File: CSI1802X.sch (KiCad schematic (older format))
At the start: 19 parts

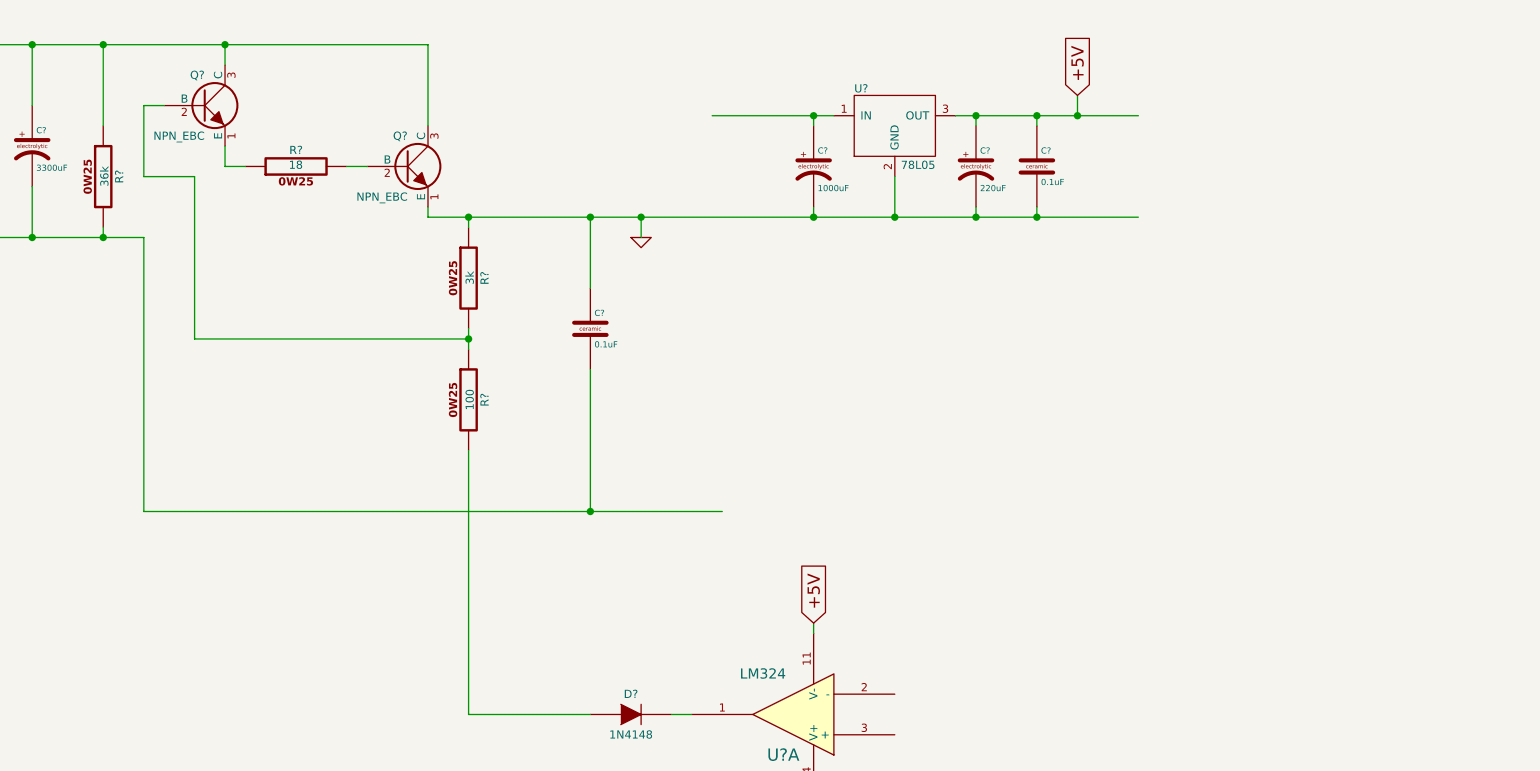
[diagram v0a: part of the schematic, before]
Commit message: -5V rail.
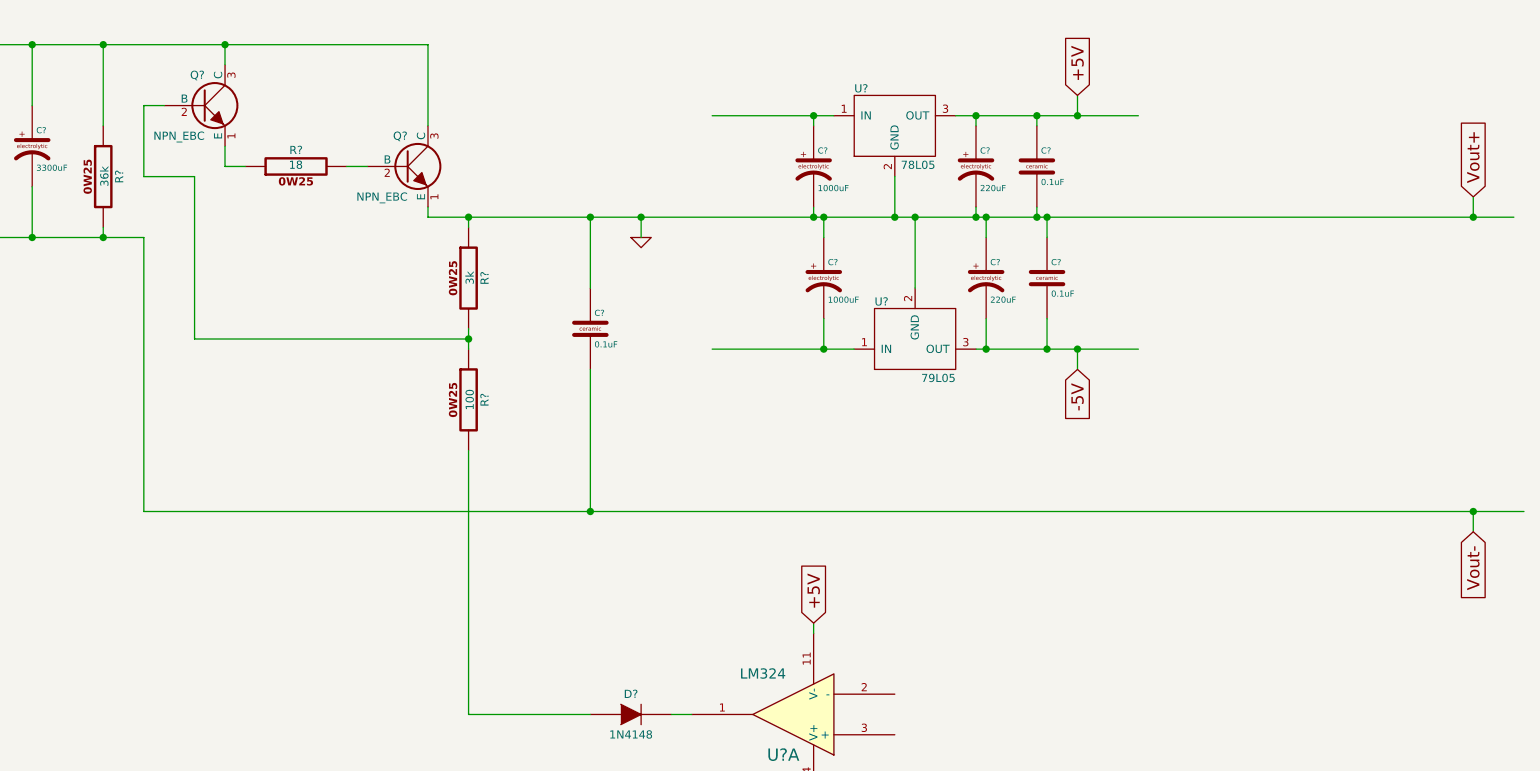
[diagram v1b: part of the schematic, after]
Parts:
- added C?: 1000uF, ~, symbol C_EL
- added C?: 220uF, ~, symbol C_EL
- added C?: 0.1uF, ~, symbol C_CER
- added U?: 79L05, ~, symbol 79L05
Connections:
- net labels added: -5V, Vout+, Vout-
- wire segments 51 -> 63
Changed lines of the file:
@@
 $EndComp
 Wire Wire Line
-	6200 2650 9700 2650
+	6200 2650 11550 2650
 $Comp
 L C_CER C?
@@
 Connection ~ 7000 2650
 Wire Wire Line
-	4800 4100 7650 4100
+	4800 4100 11600 4100
 Wire Wire Line
 	4800 2750 4800 4100
@@
 Wire Wire Line
 	8100 4700 8100 4650
+$Comp
+L 79L05 U?
+U 1 1 533A1DC9
+P 8600 3250
+F 0 "U?" H 8400 3410 40  0000 L BNN
+F 1 "79L05" H 8800 3080 40  0000 R TNN
+F 2 "~" H 8600 3250 60  0000 C CNN
+F 3 "~" H 8600 3250 60  0000 C CNN
+	1    8600 3250
+	1    0    0    -1
+$EndComp
+$Comp
+L C_EL C?
+U 1 1 533A1DD6
+P 8150 2950
+F 0 "C?" H 8170 3010 30  0000 L BNN
+F 1 "1000uF" H 8170 2860 30  0000 L TNN
+F 2 "~" H 8188 2800 30  0000 C CNN
+F 3 "~" H 8150 2950 60  0000 C CNN
+	1    8150 2950
+	1    0    0    -1
+$EndComp
+$Comp
+L C_EL C?
+U 1 1 533A1DE6
+P 8950 2950
+F 0 "C?" H 8970 3010 30  0000 L BNN
+F 1 "220uF" H 8970 2860 30  0000 L TNN
+F 2 "~" H 8988 2800 30  0000 C CNN
+F 3 "~" H 8950 2950 60  0000 C CNN
+	1    8950 2950
+	1    0    0    -1
+$EndComp
+$Comp
+L C_CER C?
+U 1 1 533A1DEC
+P 9250 2950
+F 0 "C?" H 9270 3010 30  0000 L BNN
+F 1 "0.1uF" H 9270 2890 30  0000 L TNN
+F 2 "~" H 9288 2800 30  0000 C CNN
+F 3 "~" H 9250 2950 60  0000 C CNN
+	1    9250 2950
+	1    0    0    -1
+$EndComp
+Wire Wire Line
+	8300 3300 7600 3300
+Wire Wire Line
+	8900 3300 9700 3300
+Wire Wire Line
+	9250 2750 9250 2650
+Connection ~ 9250 2650
+Wire Wire Line
+	8950 2750 8950 2650
+Connection ~ 8950 2650
+Wire Wire Line
+	8150 2750 8150 2650
+Connection ~ 8150 2650
+Wire Wire Line
+	8150 3150 8150 3300
+Connection ~ 8150 3300
+Wire Wire Line
+	8950 3150 8950 3300
+Connection ~ 8950 3300
+Wire Wire Line
+	9250 3150 9250 3300
+Connection ~ 9250 3300
+Text GLabel 9400 3400 3    60   Input ~ 0
+-5V
+Wire Wire Line
+	9400 3400 9400 3300
+Connection ~ 9400 3300
+Wire Wire Line
+	8600 3000 8600 2650
+Connection ~ 8600 2650
+Text GLabel 11350 2550 1    60   Input ~ 0
+Vout+
+Wire Wire Line
+	11350 2550 11350 2650
+Connection ~ 11350 2650
+Text GLabel 11350 4200 3    60   Input ~ 0
+Vout-
+Wire Wire Line
+	11350 4200 11350 4100
+Connection ~ 11350 4100
 $EndSCHEMATC

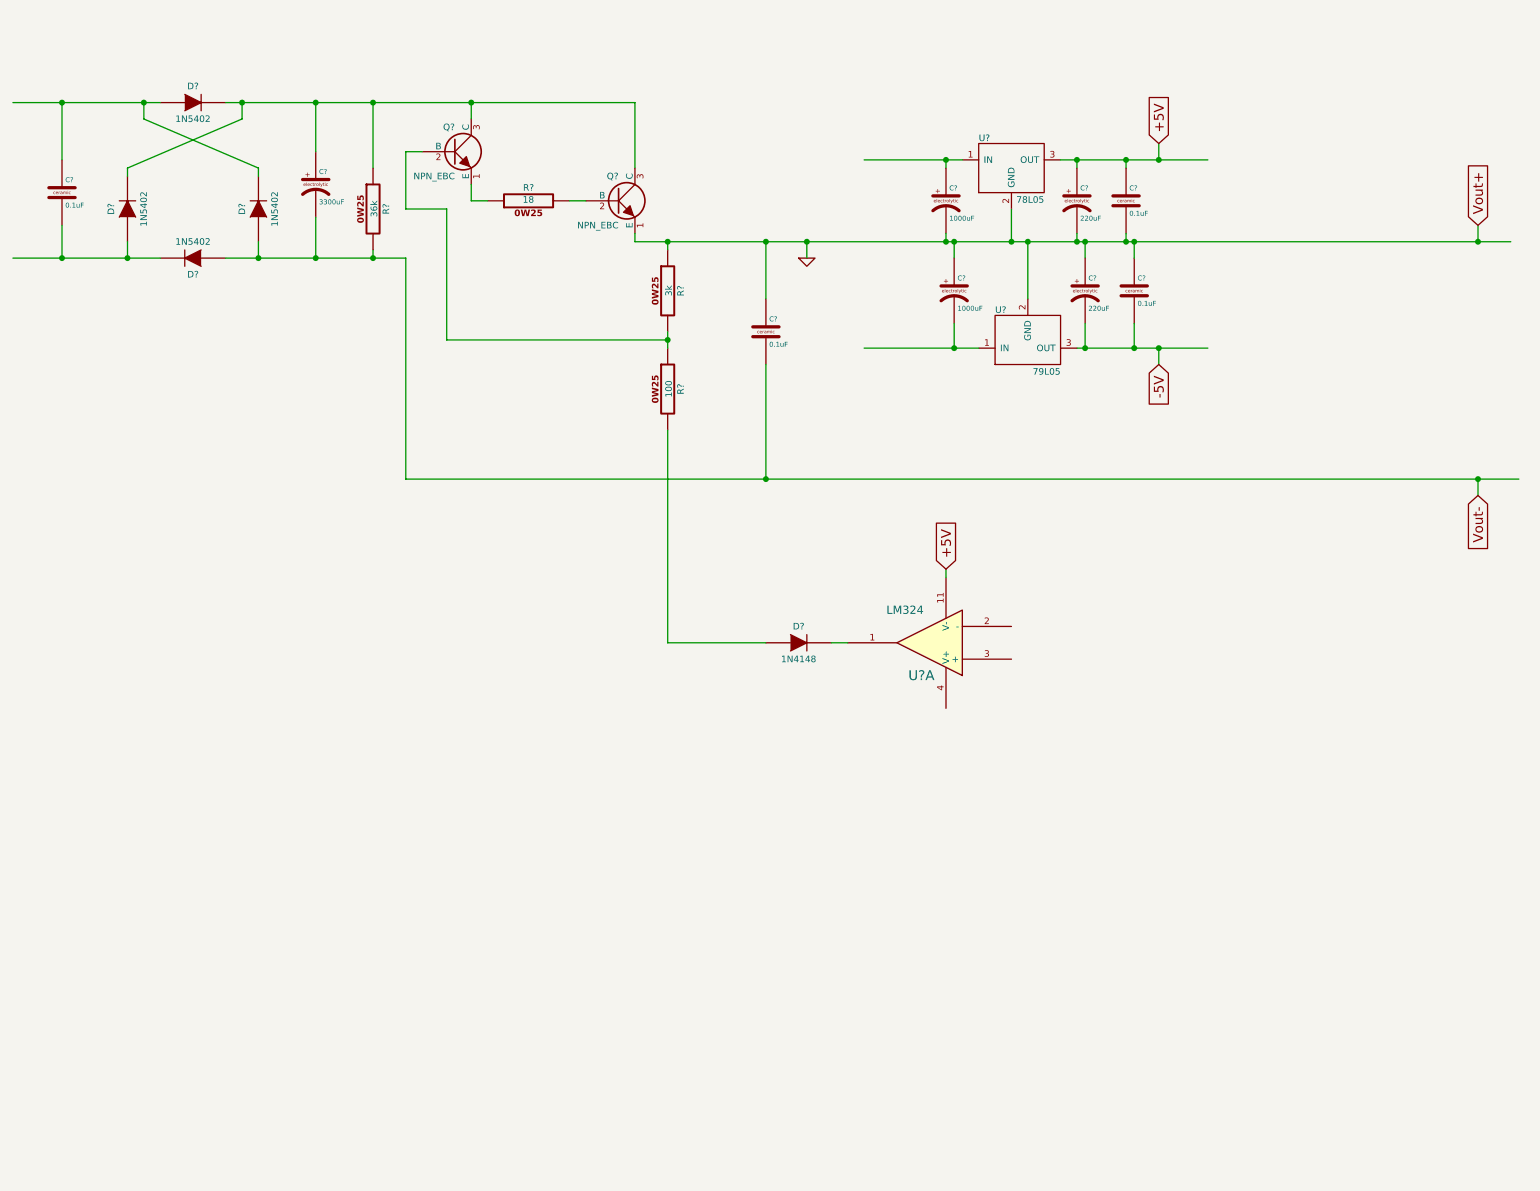
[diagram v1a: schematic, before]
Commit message: fleshing out op amp section
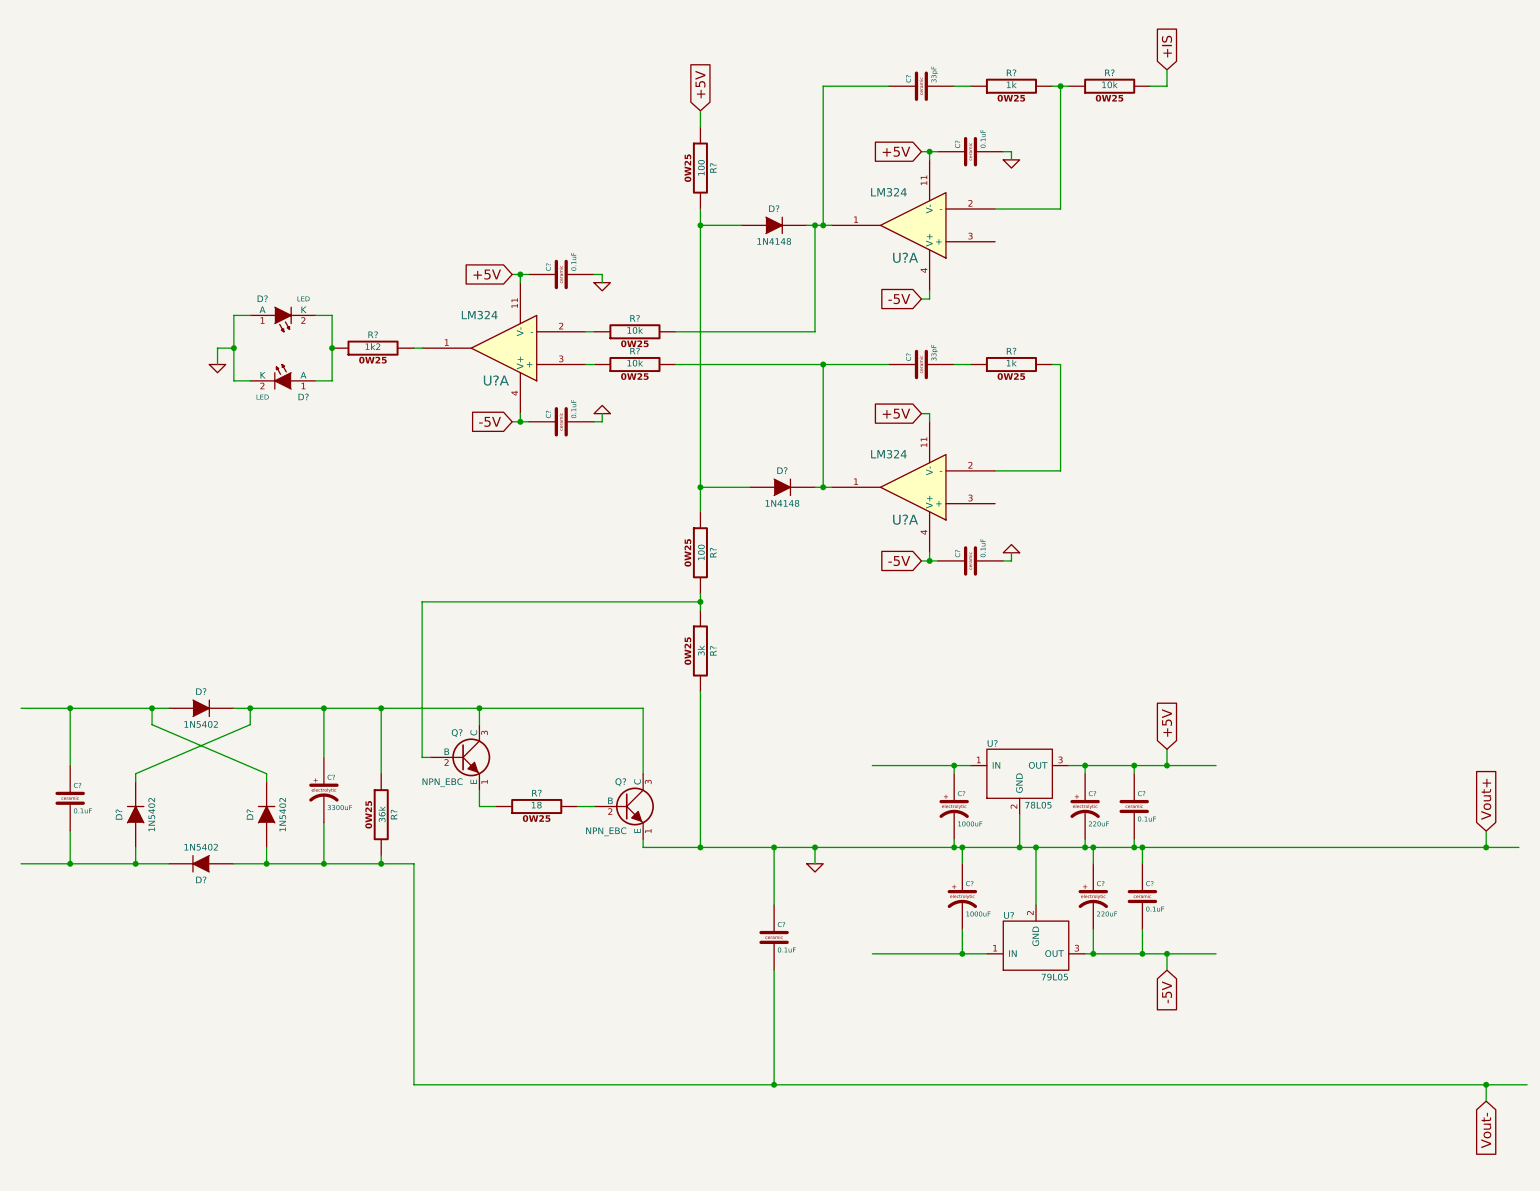
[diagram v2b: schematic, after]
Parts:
- added C? (x4): 0.1uF, ~, symbol C_CER
- added C? (x2): 33pF, ~, symbol C_CER
- added D?: 1N4148, ~, symbol DIODE
- added D? (x2): LED, ~, symbol LED
- added R?: 100, ~, symbol R_0W25
- added R? (x3): 10k, ~, symbol R_0W25
- added R? (x2): 1k, ~, symbol R_0W25
- added R?: 1k2, ~, symbol R_0W25
- added U? (x2): LM324, symbol LM324
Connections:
- net labels added: +IS
- wire segments 63 -> 110
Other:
- moved on the sheet: C?, D?, Q?, R?, U?, U?A

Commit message: fleshing out resistive dividers
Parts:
- added C?: 220uF, ~, symbol C_EL
- added C? (x3): 0.1uF, ~, symbol C_CER
- added D?: 1N4007, ~, symbol DIODE
- added R?: 0.1, ~, symbol R_0W25
- added R? (x5): 10k, ~, symbol R_0W25
- added R? (x2): 820, ~, symbol R_0W25
- added R? (x2): 180, ~, symbol R_0W25
- added R? (x2): 4k7, ~, symbol R_0W25
- added R?: 3k9, ~, symbol R_0W25
- added R?: 1k8, ~, symbol R_0W25
- added RV? (x2): 10k, ~, symbol POT
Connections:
- net labels added: +VS, -VS, REF
- net labels removed: Vout+, Vout-
- wire segments 110 -> 154
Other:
- moved on the sheet: C?, R?, U?

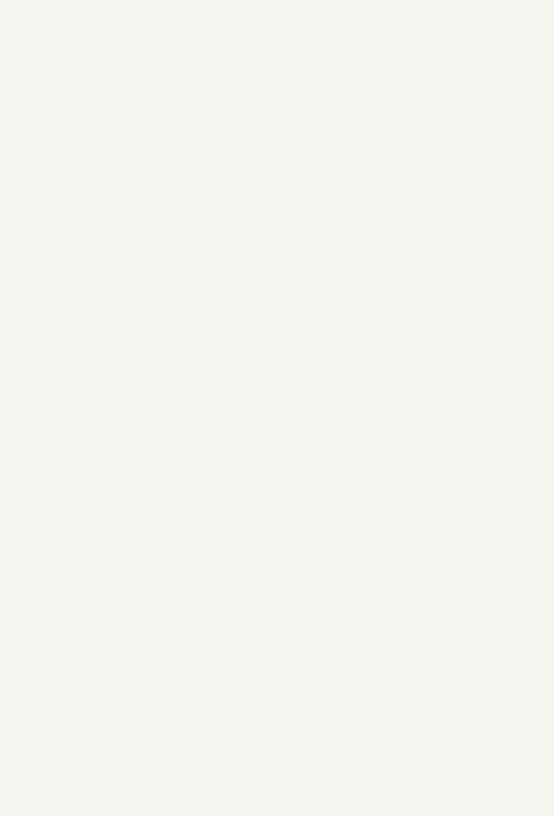
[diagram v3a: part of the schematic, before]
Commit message: TL431 regulator (REF)
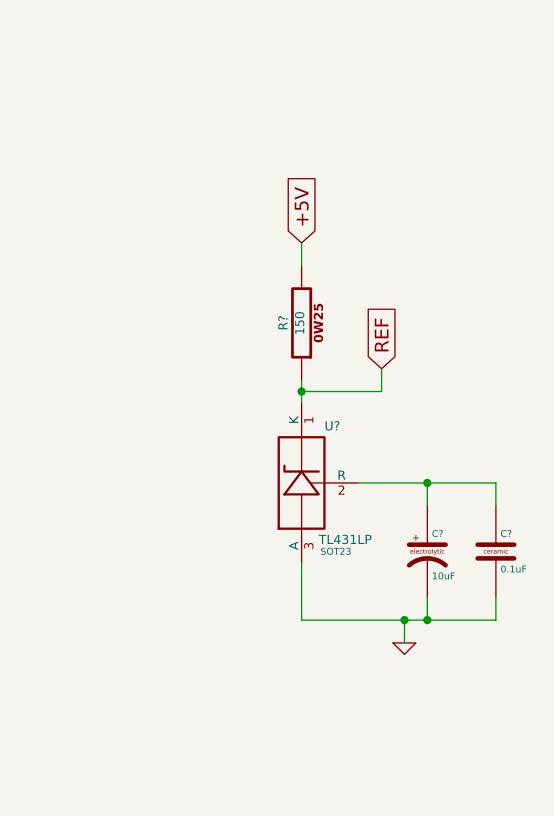
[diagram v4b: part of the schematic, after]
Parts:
- added C?: 10uF, ~, symbol C_EL
- added C?: 0.1uF, ~, symbol C_CER
- added R?: 150, ~, symbol R_0W25
- added U?: TL431LP, SOT23, symbol TL431LP
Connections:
- wire segments 154 -> 166
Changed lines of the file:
@@
 Wire Wire Line
 	12200 3450 12200 3400
+$Comp
+L TL431LP U?
+U 1 1 533A7045
+P 14850 4850
+F 0 "U?" H 14950 5075 40  0000 L BNN
+F 1 "TL431LP" H 14925 4625 40  0000 L TNN
+F 2 "SOT23" H 15000 4550 30  0000 C CNN
+F 3 "" H 14850 4850 60  0000 C CNN
+	1    14850 4850
+	1    0    0    -1
+$EndComp
+$Comp
+L C_EL C?
+U 1 1 533A7057
+P 15400 5150
+F 0 "C?" H 15420 5210 30  0000 L BNN
+F 1 "10uF" H 15420 5060 30  0000 L TNN
+F 2 "~" H 15438 5000 30  0000 C CNN
+F 3 "~" H 15400 5150 60  0000 C CNN
+	1    15400 5150
+	1    0    0    -1
+$EndComp
+$Comp
+L C_CER C?
+U 1 1 533A705D
+P 15700 5150
+F 0 "C?" H 15720 5210 30  0000 L BNN
+F 1 "0.1uF" H 15720 5090 30  0000 L TNN
+F 2 "~" H 15738 5000 30  0000 C CNN
+F 3 "~" H 15700 5150 60  0000 C CNN
+	1    15700 5150
+	1    0    0    -1
+$EndComp
+$Comp
+L R_0W25 R?
+U 1 1 533A7063
+P 14850 4150
+F 0 "R?" V 14930 4150 40  0000 C CNN
+F 1 "150" V 14857 4151 40  0000 C CNN
+F 2 "~" V 14780 4150 30  0000 C CNN
+F 3 "~" H 14850 4150 30  0000 C CNN
+	1    14850 4150
+	-1   0    0    1
+$EndComp
+Wire Wire Line
+	14850 5200 14850 5450
+Wire Wire Line
+	14850 5450 15700 5450
+Wire Wire Line
+	15700 5450 15700 5350
+Wire Wire Line
+	15400 5350 15400 5450
+Connection ~ 15400 5450
+$Comp
+L GND #PWR?
+U 1 1 533A7236
+P 15300 5550
+F 0 "#PWR?" H 15300 5550 30  0001 C CNN
+F 1 "GND" H 15300 5480 30  0001 C CNN
+F 2 "" H 15300 5550 60  0000 C CNN
+F 3 "" H 15300 5550 60  0000 C CNN
+	1    15300 5550
+	1    0    0    -1
+$EndComp
+Wire Wire Line
+	15300 5450 15300 5550
+Connection ~ 15300 5450
+Wire Wire Line
+	15100 4850 15700 4850
+Wire Wire Line
+	15400 4850 15400 4950
+Wire Wire Line
+	15700 4850 15700 4950
+Connection ~ 15400 4850
+Wire Wire Line
+	14850 4500 14850 4400
+Text GLabel 15200 4350 1    60   Input ~ 0
+REF
+Wire Wire Line
+	14850 4450 15200 4450
+Wire Wire Line
+	15200 4450 15200 4350
+Connection ~ 14850 4450
+Text GLabel 14850 3800 1    60   Input ~ 0
++5V
+Wire Wire Line
+	14850 3900 14850 3800
 $EndSCHEMATC

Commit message: pulling in relays lib
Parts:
- R?: value 820 -> 510
- R?: value 180 -> 510
- R?: value 10k -> 130
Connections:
- wire segments 166 -> 168
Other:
- moved on the sheet: C?, D?, R?

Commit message: working on bridge rectifiers and transformers
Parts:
- added D?: BRIDGE, ~, symbol BRIDGE
- added K?: RELAY_1_FORM_C, ~, symbol RELAY_1_FORM_C
- added T? (x2): TRANSFO4, ~, symbol TRANSFO4
- Q?: value NPN_EBC -> D880
- Q?: value NPN_EBC -> TIP3055
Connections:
- wire segments 168 -> 253
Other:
- note added: "FIXME: implement the 12v regulator"
- moved on the sheet: C?, D?, Q?, R?, RV?, U?, U?A

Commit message: fleshing out 12v rail
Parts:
- added C? (x2): 220uF, ~, symbol C_EL
- added C?: 47uF, ~, symbol C_EL
- added D?: BRIDGE, ~, symbol BRIDGE
- added D?: 1N5402, ~, symbol DIODE
- added Q?: D880, ~, symbol NPN_EBC
- added R?: 560, ~, symbol R_0W25
- added R?: 360, ~, symbol R_0W25
- added T?: TRANSFO, ~, symbol TRANSFO
- added U?: 78L12, ~, symbol 78L05
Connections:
- net -VS: now also C?.2, R?.2
- net +12V: now reaches K?.2 (COIL+)
- net +12V: now also C?.1, D?.2 (K), R?.2, U?.3 (OUT)
- net COIL-: now reaches K?.5 (COIL-)
- net COIL-: now also D?.1 (A), Q?.3 (C)
- new net: C?.1, D?.3 (+), U?.1 (IN)
- new net: C?.2, C?.2, D?.4 (-), Q?.1 (E), U?.2 (GND)
- new net: D?.1 (AC+), T?.4 (SB)
- new net: D?.2 (AC-), T?.3 (SA)
- new net: C?.1, Q?.2 (B), R?.1, R?.1
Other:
- note removed: "FIXME: implement the 12v regulator"
- moved on the sheet: C?, D?, K?, Q?, R?, RV?, T?, U?, U?A

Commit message: rearranging 12v rail
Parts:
- removed R?: 0.1, ~, symbol R_0W25
- added R?: 0.1, ~, symbol R
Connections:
- net +IS: now also R?.1
- net -VS: now also R?.1; no longer R?.2
- net GND: now also R?.2
- net at C?.1, Q?.2 (B), R?.1: now also R?.2; no longer R?.1
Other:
- moved on the sheet: C?, D?, K?, Q?, R?, RV?, T?, U?, U?A
